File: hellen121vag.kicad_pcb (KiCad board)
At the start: 4 copper layers, 164 x 118 mm, 99 parts, among them J21 Conn_01x05_Male, J22 USB_B_Mini, M1 Module-power_12and5V-0.3, M2 Module-knock-0.2, M3 Module-vr-discrete-0.5, M4 Module-vr-max9924-0.1, M5 Module-wbo-0.5, M6 Module:mega-mcu100/0.3, M7 Module-can-0.1, M8 Module-motor-driver-0.1, P1 368255-2, Q1 ISL9V3040D3ST, Q2 ISL9V3040D3ST, Q3 ISL9V3040D3ST, Q4 ISL9V3040D3ST, Q5 ISL9V3040D3ST, Q6 ISL9V3040D3ST, U10 BTS6143D, U11 VNLD5160TR-E, U3 VNLD5160TR-E, U4 VNLD5160TR-E, U5 VNLD5160TR-E, U6 VNLD5160TR-E, U7 VNLD5160TR-E, U8 MAX31855KASA, U9 VNLD5160TR-E

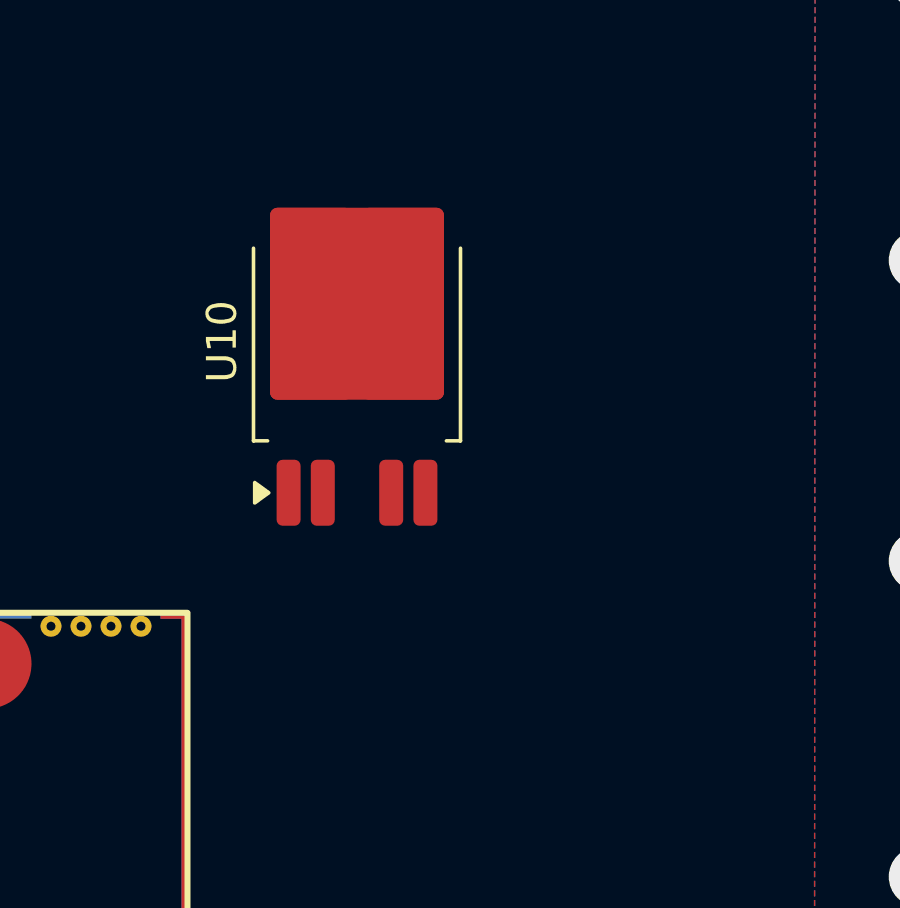
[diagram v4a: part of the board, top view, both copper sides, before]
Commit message: colocacion de componentes 100%
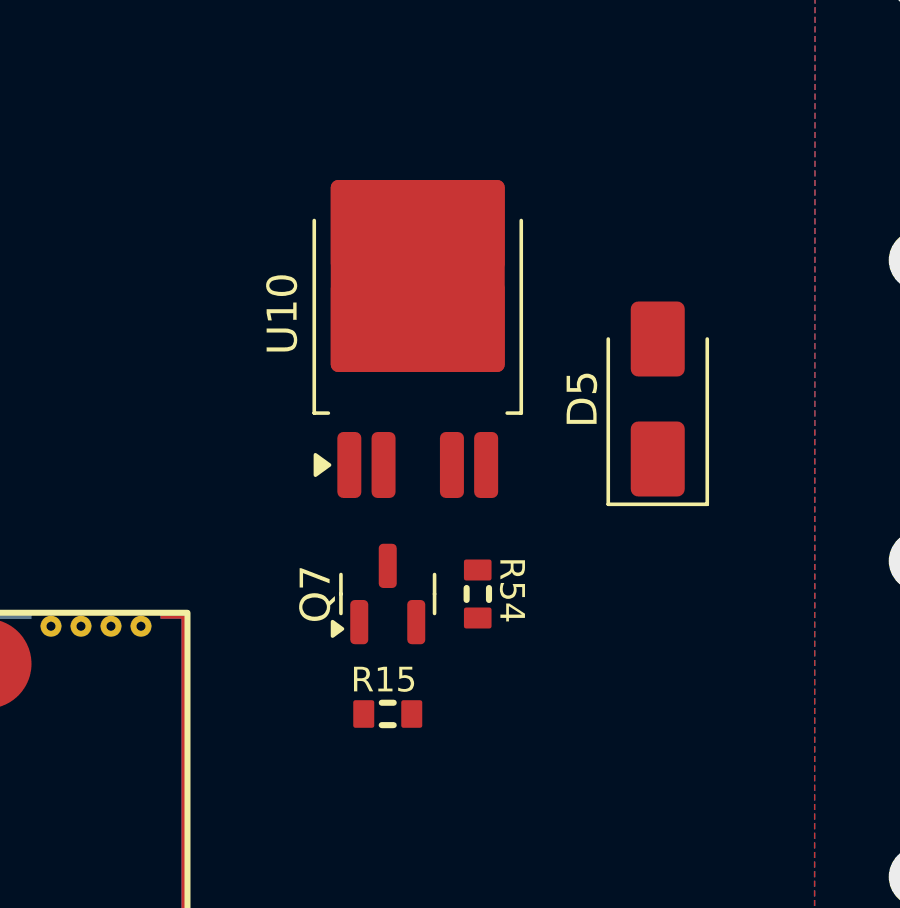
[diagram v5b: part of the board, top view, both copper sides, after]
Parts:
- added D5: SS34, Diode_SMD:D_SMA, F.Cu at (198.0, 27.0)
- added Q7: AO3400A, Package_TO_SOT_SMD:SOT-23, F.Cu at (189.0, 33.5)
- added R15: 4.7k, hellen-one-common:R0603, F.Cu at (189.0, 37.5)
- added R54: 1k, hellen-one-common:R0603, F.Cu at (192.0, 33.5)
- moved U10 2.23 mm to (190.0, 24.2)
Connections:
- D1 pad 1: +12V_RAW -> PIN117
- D2 pad 1: +12V_RAW -> PIN117
- D3 pad 1: +12V_RAW -> PIN117
- D4 pad 1: +12V_RAW -> PIN117
- F2 pad 2: +12V_RAW -> PIN117
- M1 pad V3: +12V_RAW -> PIN117
- M2 pad W1: /IN_KNOCK_RAW -> PIN81
- M5 pad E2: PIN96 -> PIN104
- M5 pad E4: /5_WBO_Rtrim -> PIN102
- M5 pad E5: PIN121 -> PIN119
- M6 pad N14a: unconnected-(M6-LED_GREEN-PadN14a) -> Net-(M6-LED_GREEN)
- M6 pad S2: PIN113 -> PIN34
- M6 pad S3: PIN113 -> PIN35
- M6 pad S4: PIN113 -> PIN36
- M6 pad S9: PIN113 -> PIN39
- U10 pad 1: Net-(U10-OUT-Pad1) -> PIN43
- U10 pad 2: unconnected-(U10-IN-Pad2) -> Net-(Q7-D)
- U10 pad 3: unconnected-(U10-Vbb-Pad3) -> PIN120
- U10 pad 4: unconnected-(U10-IS-Pad4) -> Net-(U10-IS)
- U10 pad 5: Net-(U10-OUT-Pad1) -> PIN43
